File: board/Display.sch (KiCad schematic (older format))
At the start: 7 parts, among them T1 2N7002

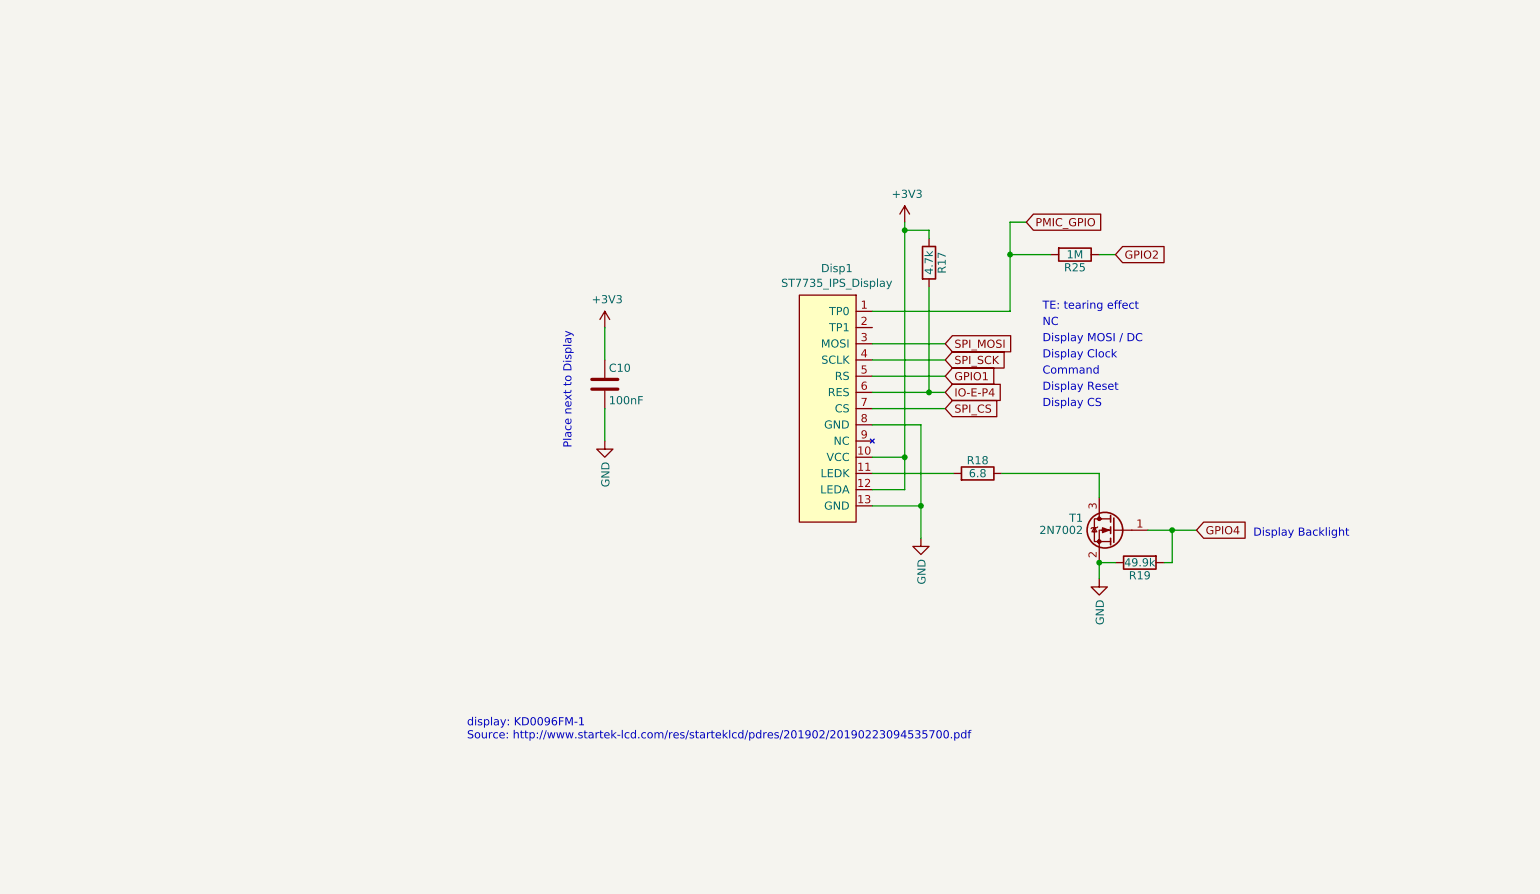
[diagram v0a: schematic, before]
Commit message: added part lib for LT1935 footprint
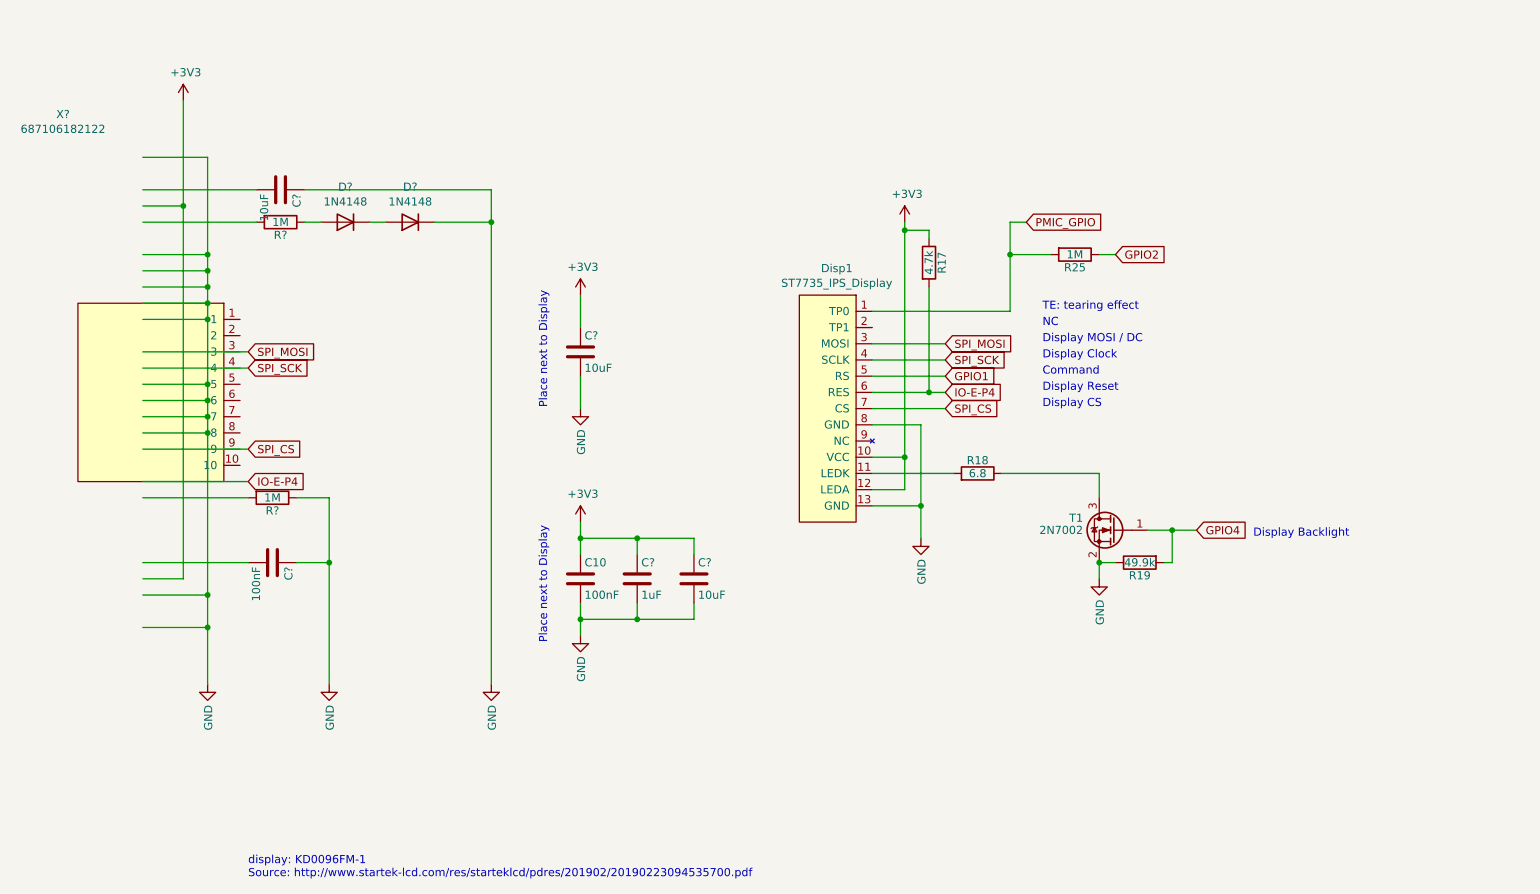
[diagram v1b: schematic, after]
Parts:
- added C?: 1uF, Capacitor_SMD:C_0201_0603Metric, symbol Device:C
- added C? (x3): 10uF, Capacitor_SMD:C_0201_0603Metric, symbol Device:C
- added C?: 100nF, Capacitor_SMD:C_0201_0603Metric, symbol Device:C
- added D? (x2): 1N4148, Diode_THT:D_DO-35_SOD27_P7.62mm_Horizontal, symbol Diode:1N4148
- added R? (x2): 1M, Resistor_SMD:R_0201_0603Metric, symbol Device:R
- added X?: 687106182122, symbol 687106182122:687106182122
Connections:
- wire segments 35 -> 93
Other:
- moved on the sheet: C10

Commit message: worked on schematics: - added new display - delete unwanted parts
Work on PCB:
- cleaned old pcb routes
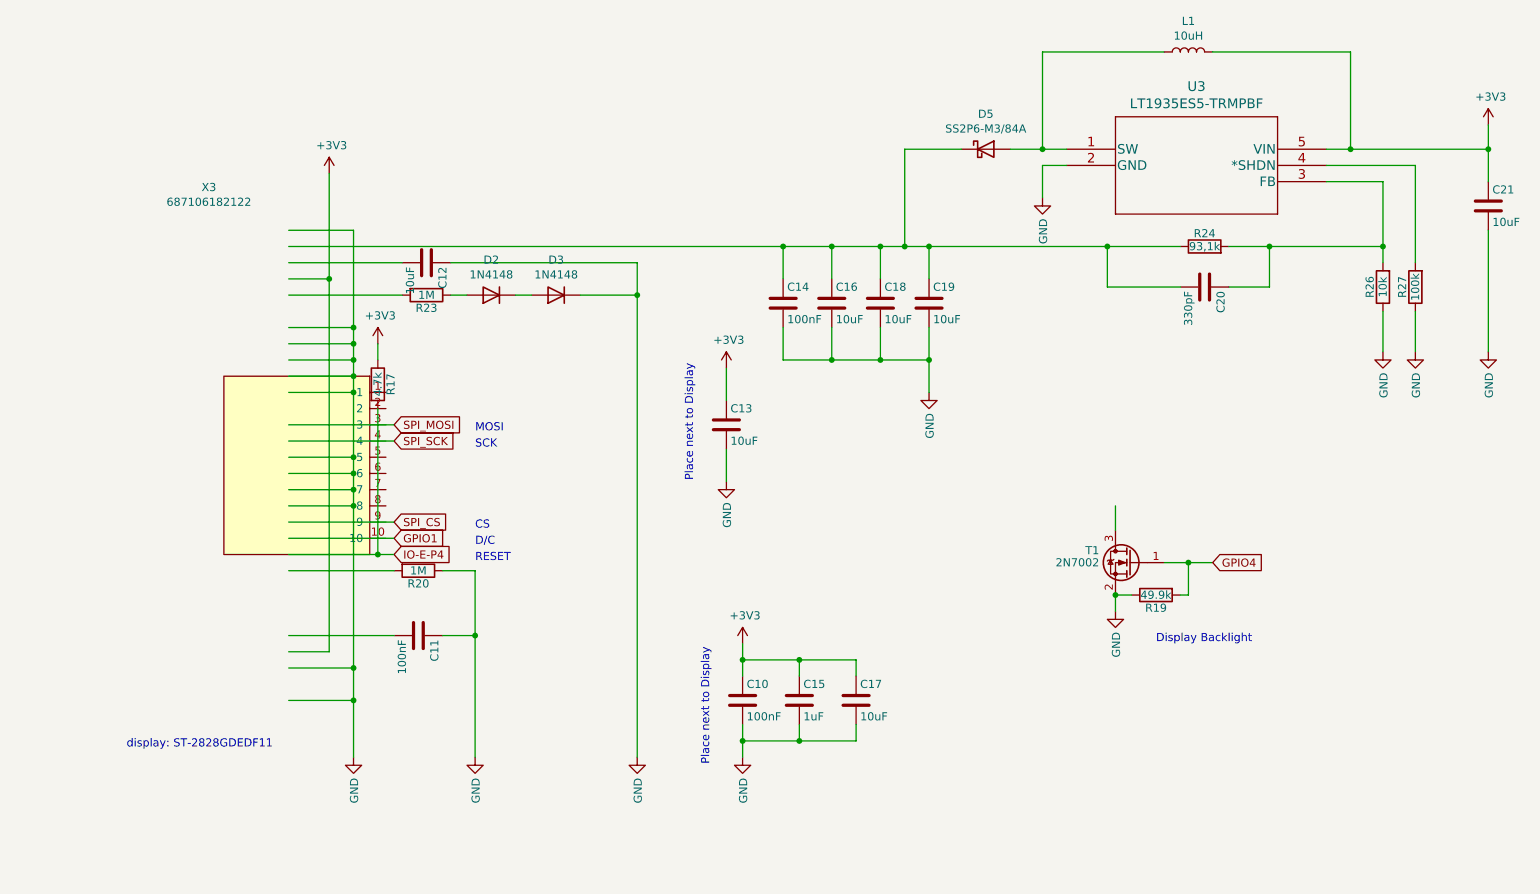
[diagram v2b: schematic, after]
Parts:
- removed Disp1: ST7735_IPS_Display, china:KD0096FM-1, symbol 0.96_IPS_display_china:ST7735_IPS_Display
- removed R18: 6.8, Resistor_SMD:R_0402_1005Metric, symbol Device:R
- removed R25: 1M, Resistor_SMD:R_0201_0603Metric, symbol Device:R
- added C14: 100nF, Capacitor_SMD:C_0201_0603Metric, symbol Device:C
- added C16, C18, C19, C21: 10uF, Capacitor_SMD:C_0201_0603Metric, symbol Device:C
- added C20: 330pF, Capacitor_SMD:C_0201_0603Metric, symbol Device:C
- added D5: SS2P6-M3/84A, symbol Device:D_Schottky
- added L1: 10uH, Inductor_SMD:L_0805_2012Metric_Pad1.15x1.40mm_HandSolder, symbol Device:L
- added R24: 93,1k, Resistor_SMD:R_0201_0603Metric, symbol Device:R
- added R26: 10k, Resistor_SMD:R_0201_0603Metric, symbol Device:R
- added R27: 100k, Resistor_SMD:R_0201_0603Metric, symbol Device:R
- added U3: LT1935ES5-TRMPBF, LT1935:LT1935ES5-TRMPBF, symbol LT1935:LT1935ES5-TRMPBF
- D2, D3: renamed from D?; footprint Diode_THT:D_DO-35_SOD27_P7.62mm_Horizontal -> Diode_SMD:D_SOD-123
- gave numbers to parts that had none: 8
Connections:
- net labels removed: GPIO2, PMIC_GPIO
- wire segments 93 -> 118
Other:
- note added: "CS"
- note added: "D/C"
- note added: "MOSI"
- note added: "RESET"
- note added: "SCK"
- note added: "display: ST-2828GDEDF11"
- note removed: "Command"
- note removed: "Display CS"
- note removed: "Display Clock"
- note removed: "Display MOSI / DC"
- note removed: "Display Reset"
- note removed: "NC"
- note removed: "TE: tearing effect"
- note removed: "display: KD0096FM-1\nSource: http://www.startek-lcd.com/res/starteklcd/pdres/201902/20190223094535700.pdf"
- moved on the sheet: C10, C11, C12, C13, C15, C17, D2, D3, R17, R19, R20, R23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

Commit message: - Added connector lib - added footprint for schottkey diode - added keep-out for new display
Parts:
- removed R19: 49.9k, Resistor_SMD:R_0201_0603Metric, symbol Device:R
- removed T1: 2N7002, Package_TO_SOT_SMD:SOT-323_SC-70, symbol Transistor_FET:2N7002
- removed X3: 687106182122, symbol 687106182122:687106182122
- added X3: 687130182122, WR-FPC 0.50 mm SMT ZIF Horizontal Dual Contact:687130182122, symbol 687106182122:687130182122
- D5: footprint (none) -> badge:DO-220AA
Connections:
- net labels removed: GPIO4
- wire segments 118 -> 111
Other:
- note removed: "Display Backlight"
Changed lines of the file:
@@
 Comment4 ""
 $EndDescr
-Text GLabel 8550 4650 2    50   Input ~ 0
-GPIO4
-Text Notes 8200 5150 0    50   ~ 0
-Display Backlight
 $Comp
 L Device:C C10
@@
 Place next to Display
 $Comp
-L Device:R R19
-U 1 1 5CEA1C59
-P 8200 4850
-F 0 "R19" V 8280 4850 50  0000 C CNN
-F 1 "49.9k" V 8200 4850 50  0000 C CNN
-F 2 "Resistor_SMD:R_0201_0603Metric" V 8130 4850 50  0001 C CNN
-F 3 "~" H 8200 4850 50  0001 C CNN
-	1    8200 4850
-	0    -1   1    0
-$EndComp
-Wire Wire Line
-	8350 4850 8400 4850
-Wire Wire Line
-	8050 4850 7950 4850
-$Comp
-L Transistor_FET:2N7002 T1
-U 1 1 5D0832A3
-P 8050 4650
-F 0 "T1" H 8250 4725 50  0000 L CNN
-F 1 "2N7002" H 8250 4650 50  0000 L CNN
-F 2 "Package_TO_SOT_SMD:SOT-323_SC-70" H 8250 4575 50  0001 L CIN
-F 3 "https://www.fairchildsemi.com/datasheets/2N/2N7002.pdf" H 8050 4650 50  0001 L CNN
-	1    8050 4650
-	-1   0    0    -1
-$EndComp
-$Comp
-L power:GND #PWR?
-U 1 1 5D0855E5
-P 7950 4950
-AR Path="/5CB104E6/5D0855E5" Ref="#PWR?"  Part="1"
-AR Path="/5D345ECD/5D0855E5" Ref="#PWR036"  Part="1"
-F 0 "#PWR036" H 7950 4700 50  0001 C CNN
-F 1 "GND" V 7955 4822 50  0000 R CNN
-F 2 "" H 7950 4950 50  0001 C CNN
-F 3 "" H 7950 4950 50  0001 C CNN
-	1    7950 4950
-	1    0    0    -1
-$EndComp
-Wire Wire Line
-	7950 4950 7950 4850
-Connection ~ 7950 4850
-Wire Wire Line
-	7950 4450 7950 4300
-Wire Wire Line
-	8250 4650 8400 4650
-Wire Wire Line
-	8400 4650 8400 4850
-Wire Wire Line
-	8400 4650 8550 4650
-Connection ~ 8400 4650
-$Comp
-L 687106182122:687106182122 X3
-U 1 1 610A95DE
-P 2900 4050
-F 0 "X3" H 2358 5765 50  0000 C CNN
-F 1 "687106182122" H 2358 5674 50  0000 C CNN
-F 2 "" H 2600 5600 50  0001 C CNN
-F 3 "" H 2600 5600 50  0001 C CNN
-	1    2900 4050
-	1    0    0    -1
-$EndComp
-$Comp
 L power:GND #PWR?
 U 1 1 610AAA25
@@
 F 0 "D5" H 7150 2317 50  0000 C CNN
 F 1 "SS2P6-M3/84A" H 7150 2226 50  0000 C CNN
-F 2 "" H 7150 2100 50  0001 C CNN
+F 2 "badge:DO-220AA" H 7150 2100 50  0001 C CNN
 F 3 "~" H 7150 2100 50  0001 C CNN
 	1    7150 2100
@@
 Wire Wire Line
 	3400 4600 3500 4600
+$Comp
+L 687106182122:687130182122 X3
+U 1 1 610D0EF3
+P 2900 4050
+F 0 "X3" H 2358 5765 50  0000 C CNN
+F 1 "687130182122" H 2358 5674 50  0000 C CNN
+F 2 "WR-FPC 0.50 mm SMT ZIF Horizontal Dual Contact:687130182122" H 2600 5600 50  0001 C CNN
+F 3 "" H 2600 5600 50  0001 C CNN
+	1    2900 4050
+	1    0    0    -1
+$EndComp
 $EndSCHEMATC
